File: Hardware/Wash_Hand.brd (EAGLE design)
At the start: 71.1 x 48.3 mm, 90 parts, among them IC1 LM358D, IC2 LP298XS, IC3 405016TSSOP, J1 I2C, J2 ICSP, J3 SPI, J4 9V_CONN, J5 EXT_VCC, J6 6_PIN_SERIAL_CABLEPTH, J7 OP_B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

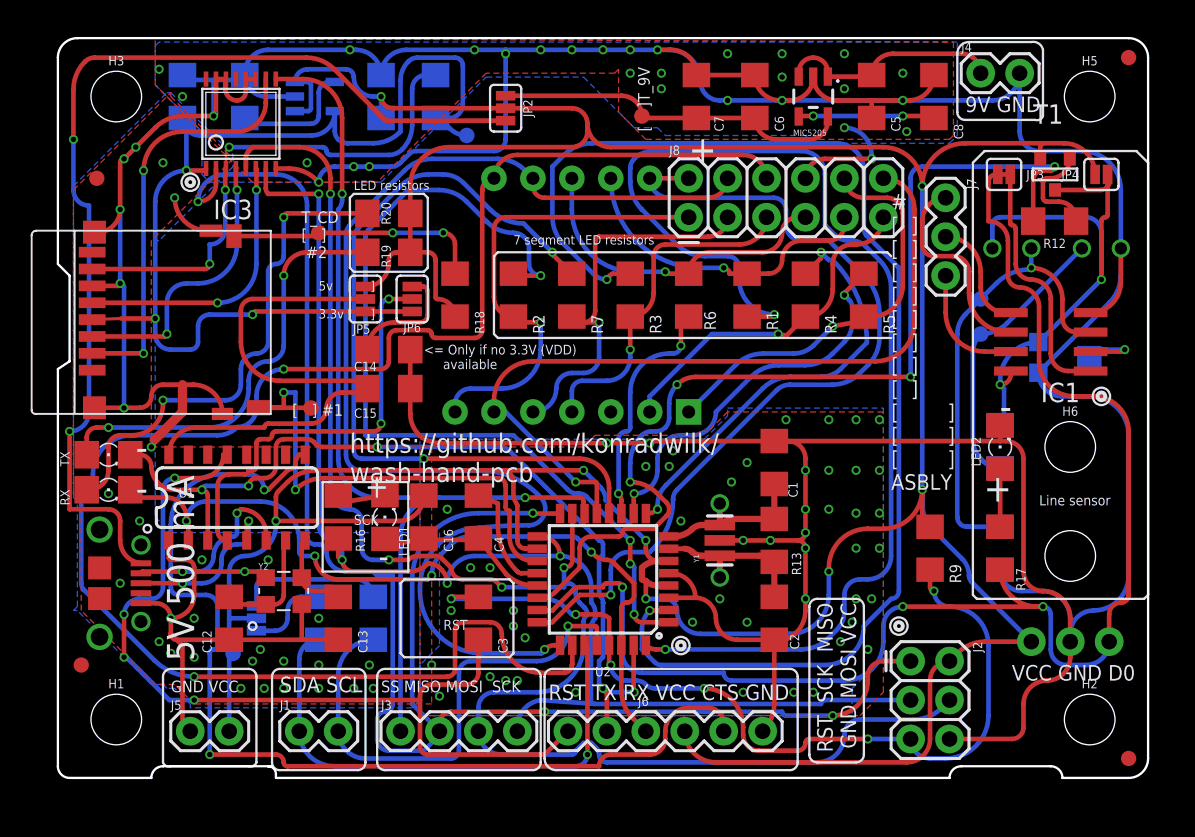
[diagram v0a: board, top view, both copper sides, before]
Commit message: Board/Design: Replace PNP with NPN
And also re-route the ground since the NPN will now
control whether this whole thing is going to be on/off.

Signed-off-by: Konrad Rzeszutek Wilk <konrad@kernel.org>
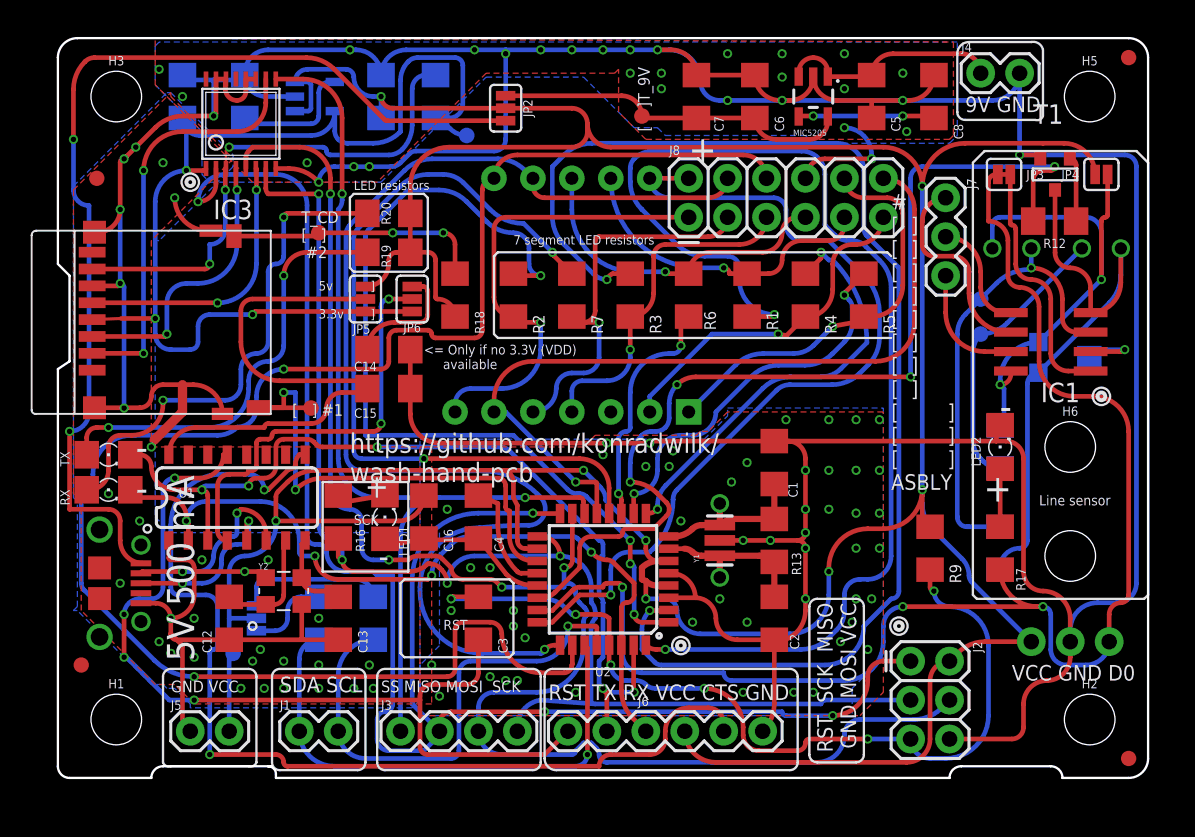
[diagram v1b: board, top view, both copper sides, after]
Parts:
- T1: value PNP -> NPN
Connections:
- net ON_OFF_PNP renamed ON_OFF_SWT
- new net NPN_COLLECTOR: E.C, IC1.4, R15.1, T1.1, TM1.1
- net 0: now also T1.2; no longer E.C, IC1.4, R15.1, TM1.1
- net VCC: no longer T1.2
- net V_POS: no longer T1.1
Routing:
- net NPN_COLLECTOR: track 0.00 -> 38.1 mm
- net 0: track 386.8 -> 374.1 mm, vias 110 -> 112
- net V_POS: track 37.2 -> 33.0 mm
- net N$16: track 6.27 -> 4.23 mm
- net VCC: track 249.0 -> 248.0 mm

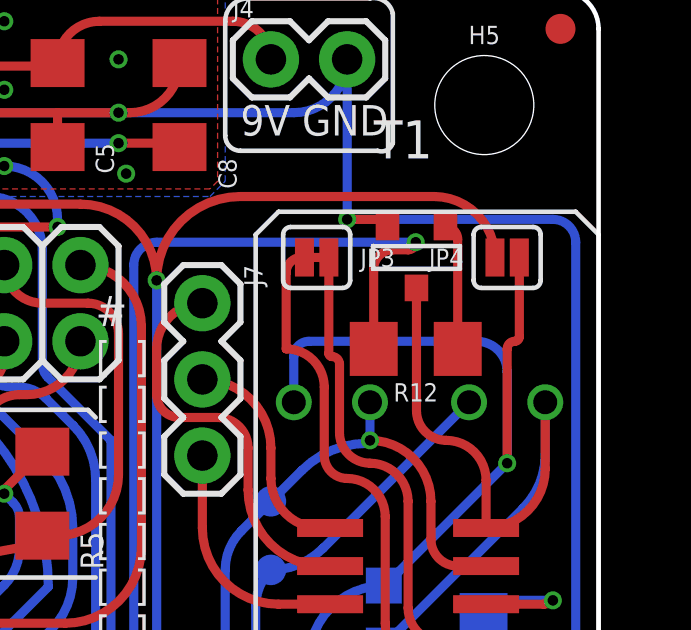
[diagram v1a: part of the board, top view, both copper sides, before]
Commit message: Board/Schematic: Add BYPASS_SWITCH
In case we do not want to use the NPN transistor.

Signed-off-by: Konrad Rzeszutek Wilk <konrad@kernel.org>
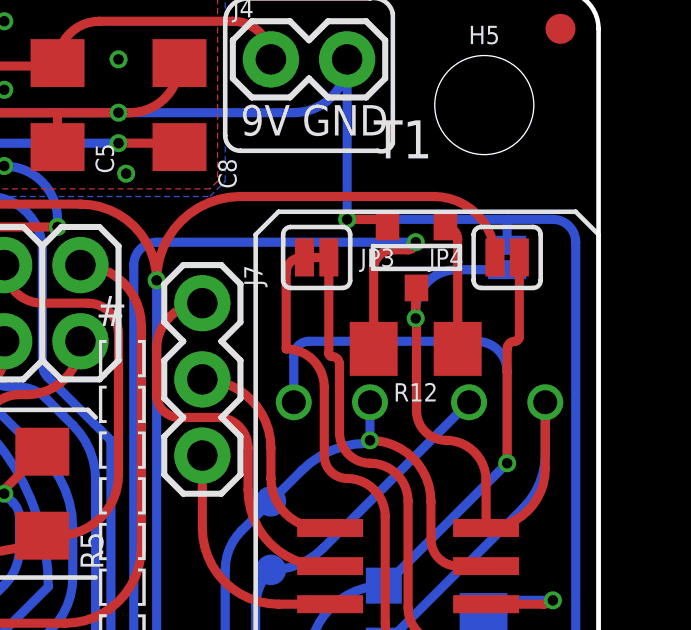
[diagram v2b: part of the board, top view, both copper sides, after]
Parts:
- added JP7: BYPASS_SWT, SparkFun-Jumpers:SMT-JUMPER_2_NO_SILK
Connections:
- net 0: now also JP7.1
- net NPN_COLLECTOR: now also JP7.2
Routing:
- net NPN_COLLECTOR: track 38.1 -> 41.9 mm, vias 0 -> 1
- net 0: track 374.1 -> 375.0 mm
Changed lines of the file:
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@@
 <layer number="27" name="tValues" color="7" fill="1" visible="yes" active="yes"/>
 <layer number="28" name="bValues" color="7" fill="1" visible="yes" active="yes"/>
-<layer number="29" name="tStop" color="7" fill="3" visible="no" active="yes"/>
-<layer number="30" name="bStop" color="7" fill="6" visible="no" active="yes"/>
-<layer number="31" name="tCream" color="7" fill="4" visible="no" active="yes"/>
-<layer number="32" name="bCream" color="7" fill="5" visible="no" active="yes"/>
-<layer number="33" name="tFinish" color="6" fill="3" visible="no" active="yes"/>
-<layer number="34" name="bFinish" color="6" fill="6" visible="no" active="yes"/>
-<layer number="35" name="tGlue" color="7" fill="4" visible="no" active="yes"/>
-<layer number="36" name="bGlue" color="7" fill="5" visible="no" active="yes"/>
-<layer number="37" name="tTest" color="7" fill="1" visible="no" active="yes"/>
-<layer number="38" name="bTest" color="7" fill="1" visible="no" active="yes"/>
+<layer number="29" name="tStop" color="7" fill="3" visible="yes" active="yes"/>
+<layer number="30" name="bStop" color="7" fill="6" visible="yes" active="yes"/>
+<layer number="31" name="tCream" color="7" fill="4" visible="yes" active="yes"/>
+<layer number="32" name="bCream" color="7" fill="5" visible="yes" active="yes"/>
+<layer number="33" name="tFinish" color="6" fill="3" visible="yes" active="yes"/>
+<layer number="34" name="bFinish" color="6" fill="6" visible="yes" active="yes"/>
+<layer number="35" name="tGlue" color="7" fill="4" visible="yes" active="yes"/>
+<layer number="36" name="bGlue" color="7" fill="5" visible="yes" active="yes"/>
+<layer number="37" name="tTest" color="7" fill="1" visible="yes" active="yes"/>
+<layer number="38" name="bTest" color="7" fill="1" visible="yes" active="yes"/>
 <layer number="39" name="tKeepout" color="4" fill="11" visible="yes" active="yes"/>
 <layer number="40" name="bKeepout" color="1" fill="11" visible="yes" active="yes"/>
@@
 <layer number="42" name="bRestrict" color="1" fill="10" visible="yes" active="yes"/>
 <layer number="43" name="vRestrict" color="2" fill="10" visible="yes" active="yes"/>
-<layer number="44" name="Drills" color="7" fill="1" visible="no" active="yes"/>
-<layer number="45" name="Holes" color="7" fill="1" visible="no" active="yes"/>
-<layer number="46" name="Milling" color="3" fill="1" visible="no" active="yes"/>
-<layer number="47" name="Measures" color="7" fill="1" visible="no" active="yes"/>
+<layer number="44" name="Drills" color="7" fill="1" visible="yes" active="yes"/>
+<layer number="45" name="Holes" color="7" fill="1" visible="yes" active="yes"/>
+<layer number="46" name="Milling" color="3" fill="1" visible="yes" active="yes"/>
+<layer number="47" name="Measures" color="7" fill="1" visible="yes" active="yes"/>
 <layer number="48" name="Document" color="7" fill="1" visible="yes" active="yes"/>
 <layer number="49" name="Reference" color="7" fill="1" visible="yes" active="yes"/>
@@
 </element>
 <element name="LOGO2" library="darnok_logo" package="HAPPY_FACE_LOGO" value="HAPPY_FACE_LOGO" x="33.528" y="44.196" smashed="yes" rot="MR0"/>
+<element name="JP7" library="SparkFun-Jumpers" library_urn="urn:adsk.eagle:library:528" package="SMT-JUMPER_2_NO_SILK" package3d_urn="urn:adsk.eagle:package:39279/1" value="BYPASS_SWT" x="68.072" y="39.37" smashed="yes" rot="MR270">
+<attribute name="NAME" x="66.929" y="39.37" size="0.6096" layer="26" font="vector" ratio="20" rot="MR270" align="bottom-center"/>
+<attribute name="VALUE" x="69.215" y="39.37" size="0.6096" layer="28" font="vector" ratio="20" rot="MR270" align="top-center"/>
+</element>
 </elements>
 <signals>
@@
 <wire x1="61.214" y1="22.758" x2="61.468" y2="23.012" width="0.3048" layer="1" curve="-90"/>
 <via x="35.56" y="21.082" extent="1-16" drill="0.35"/>
-<wire x1="62.738" y1="40.64" x2="69.596" y2="40.64" width="0.3048" layer="16"/>
+<wire x1="62.738" y1="40.64" x2="68.072" y2="40.64" width="0.3048" layer="16"/>
+<wire x1="68.072" y1="40.64" x2="69.596" y2="40.64" width="0.3048" layer="16"/>
 <wire x1="70.358" y1="39.878" x2="69.596" y2="40.64" width="0.3048" layer="16" curve="90"/>
 <wire x1="66.04" y1="8.89" x2="66.04" y2="9.652" width="0.3048" layer="16"/>
@@
 <wire x1="69.088" y1="11.43" x2="70.358" y2="12.7" width="0.3048" layer="16" curve="90"/>
 <wire x1="70.358" y1="12.7" x2="70.358" y2="39.878" width="0.3048" layer="16"/>
+<contactref element="JP7" pad="1"/>
+<wire x1="68.072" y1="39.7764" x2="68.072" y2="40.64" width="0.3048" layer="16"/>
 </signal>
 <signal name="D0">
@@
 <wire x1="69.342" y1="32.325" x2="69.342" y2="34.544" width="0.3048" layer="1"/>
 <wire x1="69.342" y1="32.802103125" x2="69.342" y2="34.544" width="0.3048" layer="16"/>
-<wire x1="65.0494" y1="38.354" x2="65.0494" y2="34.2646" width="0.3048" layer="1"/>
 <wire x1="65.0494" y1="34.2646" x2="66.04" y2="33.274" width="0.3048" layer="1" curve="90"/>
 <wire x1="66.04" y1="33.274" x2="67.37" y2="31.944" width="0.3048" layer="1" curve="-90"/>
@@
 <wire x1="63.246" y1="25.717" x2="63.961" y2="26.432" width="0.3048" layer="16" curve="-90"/>
 <wire x1="63.246" y1="15.494" x2="63.246" y2="25.717" width="0.3048" layer="16"/>
+<contactref element="JP7" pad="2"/>
+<wire x1="68.072" y1="38.9636" x2="66.3956" y2="38.9636" width="0.3048" layer="16"/>
+<wire x1="66.3956" y1="38.9636" x2="65.024" y2="37.592" width="0.3048" layer="16" curve="90"/>
+<wire x1="65.024" y1="37.592" x2="65.024" y2="37.338" width="0.3048" layer="16"/>
+<via x="65.024" y="37.338" extent="1-16" drill="0.35"/>
+<wire x1="65.024" y1="37.338" x2="65.024" y2="38.3286" width="0.3048" layer="1"/>
+<wire x1="65.024" y1="38.3286" x2="65.0494" y2="38.354" width="0.3048" layer="1" curve="-90"/>
+<wire x1="65.024" y1="37.338" x2="65.0494" y2="37.3126" width="0.3048" layer="1" curve="-90"/>
+<wire x1="65.0494" y1="37.3126" x2="65.0494" y2="34.2646" width="0.3048" layer="1"/>
 </signal>
 <signal name="N$16">
